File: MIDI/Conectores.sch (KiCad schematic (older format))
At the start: 3 parts, among them J4 CONN_01X06, J5 CONN_01X06

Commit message: Se continuan las correciones correspondientes a la 1ra revisión
> Se realizan los cambios necesarios para la utilización de la biblioteca de huellas autocontenidas.
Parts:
- J4, J5: footprint Pin_Headers:Pin_Header_Straight_1x06_Pitch2.54mm -> MIDI:Pin_Header_Straight_1x06_Pitch2.54mm
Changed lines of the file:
@@
 F 0 "J5" H 6595 2780 50  0000 C CNN
 F 1 "CONN_01X06" V 6695 2430 50  0000 C CNN
-F 2 "Pin_Headers:Pin_Header_Straight_1x06_Pitch2.54mm" H 6595 2430 50  0001 C CNN
+F 2 "MIDI:Pin_Header_Straight_1x06_Pitch2.54mm" H 6595 2430 50  0001 C CNN
 F 3 "http://portal.fciconnect.com/Comergent//fci/drawing/75915.pdf" H 6595 2430 50  0001 C CNN
 F 4 "CONN RCPT 6POS .100\" SGL PCB" H 0   0   60  0001 C CNN "Desc"
@@
 F 0 "J4" H 5045 2780 50  0000 C CNN
 F 1 "CONN_01X06" V 5145 2430 50  0000 C CNN
-F 2 "Pin_Headers:Pin_Header_Straight_1x06_Pitch2.54mm" H 5045 2430 50  0001 C CNN
+F 2 "MIDI:Pin_Header_Straight_1x06_Pitch2.54mm" H 5045 2430 50  0001 C CNN
 F 3 "http://portal.fciconnect.com/Comergent//fci/drawing/75915.pdf" H 5045 2430 50  0001 C CNN
 F 4 "CONN RCPT 6POS .100\" SGL PCB" H 0   0   60  0001 C CNN "Desc"

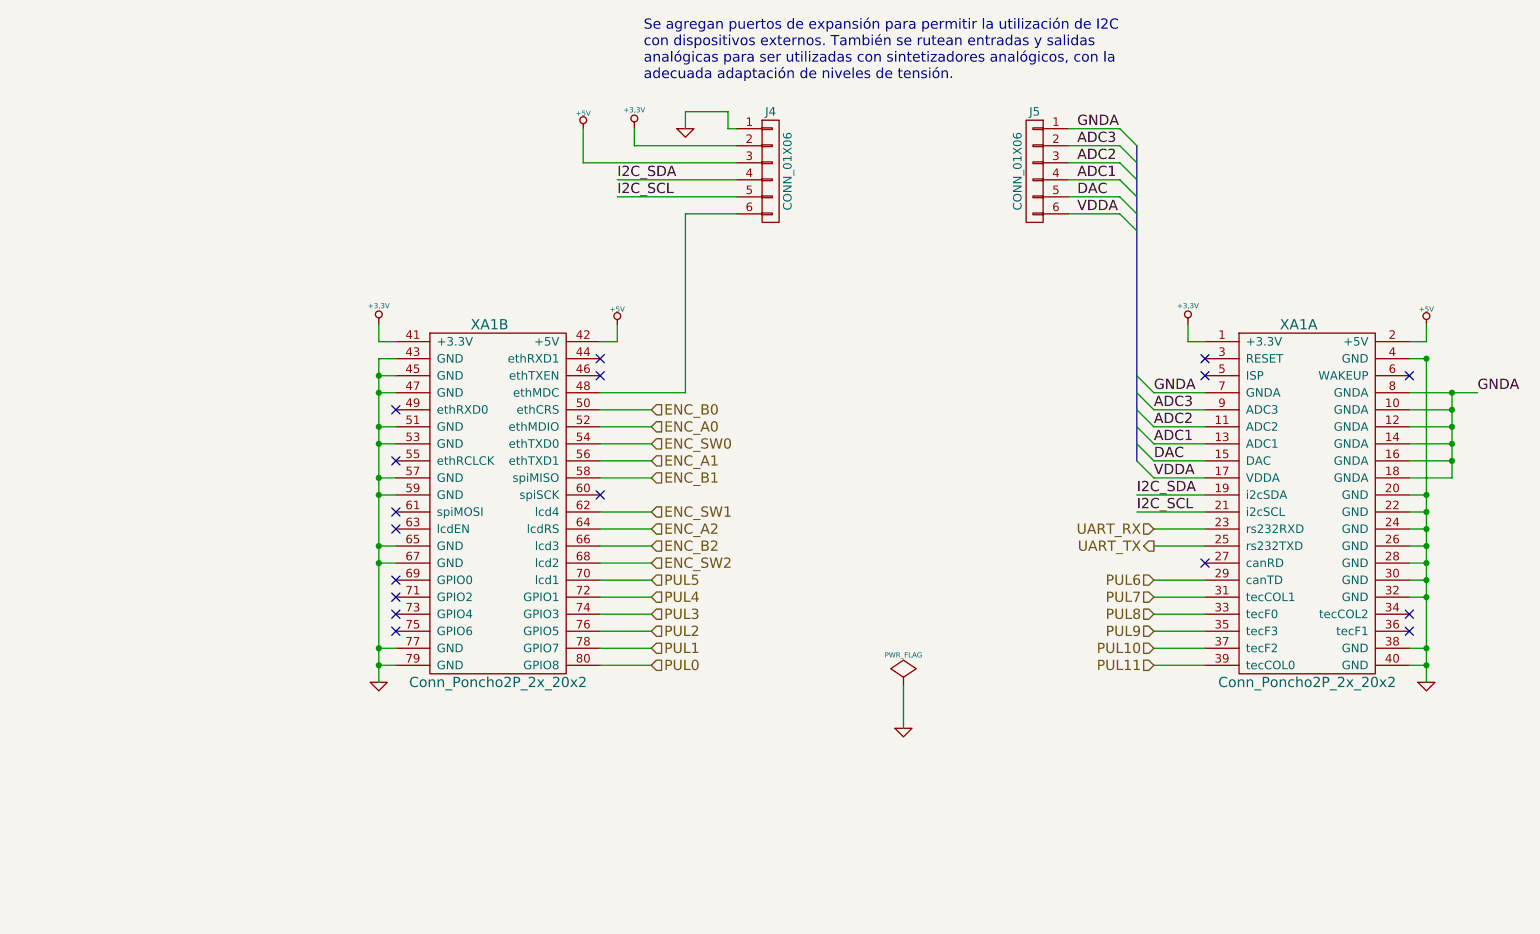
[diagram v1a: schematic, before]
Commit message: Se modifica librería para uncluir tira de pines
> Se reemplaza conector multiparte por elementos individuales para facilitar el cálculo con kiCost.
> Se incluyen modelos 3D para completar la vista 3D.
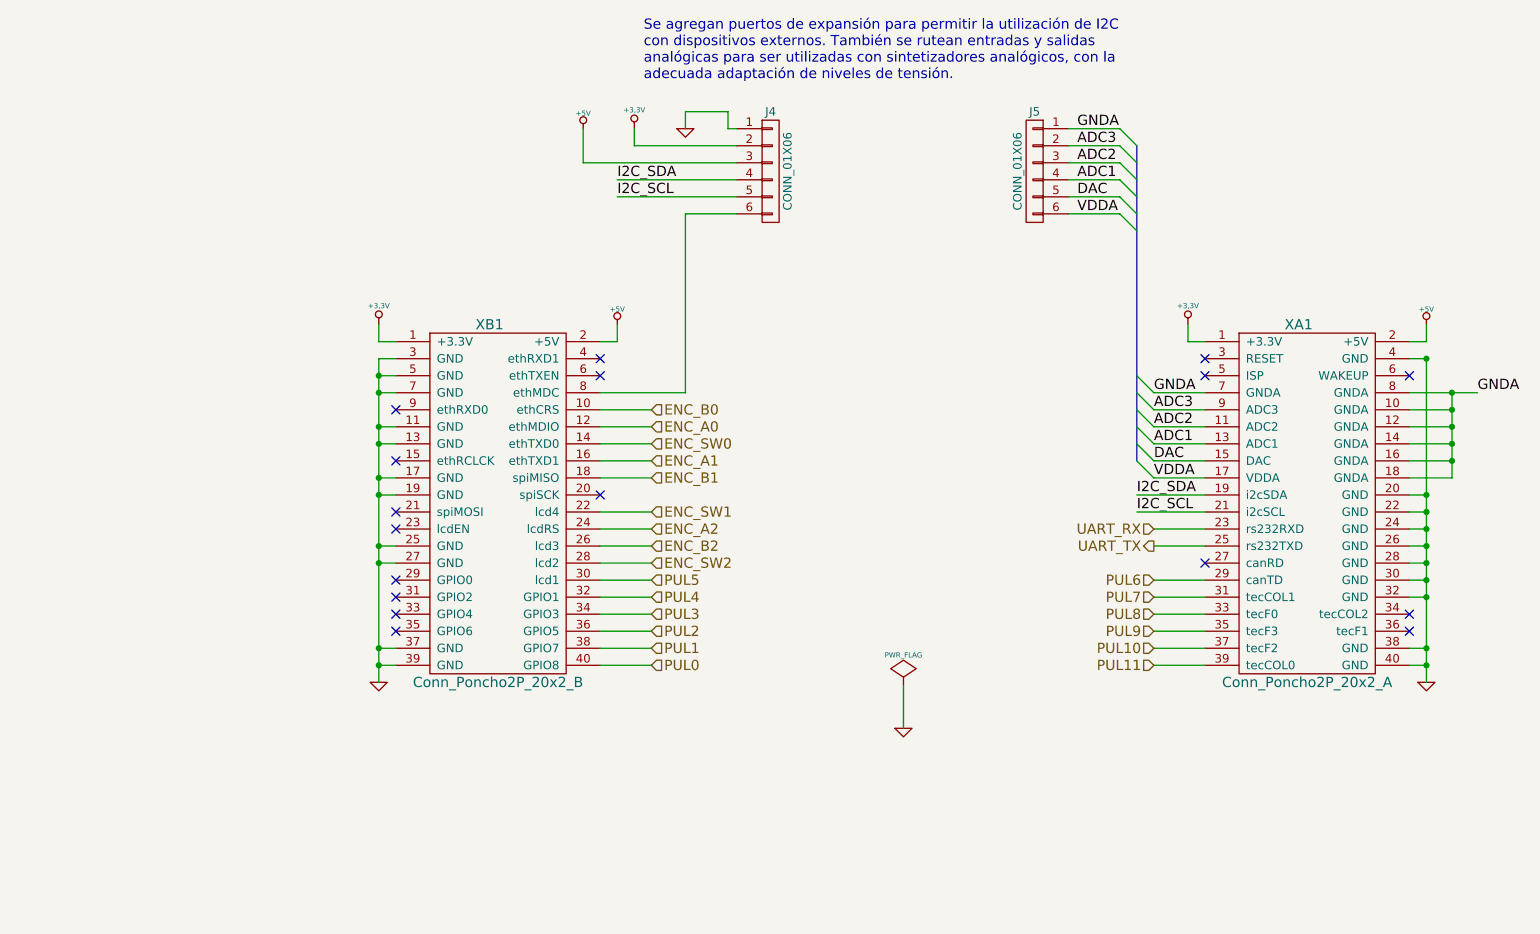
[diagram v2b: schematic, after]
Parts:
- removed XA1: Conn_Poncho2P_2x_20x2, MIDI:Conn_Poncho_Completo, symbol Conn_Poncho2P_2x_20x2
- added XA1: Conn_Poncho2P_20x2_A, MIDI:PIN_ARRAY_20X2, symbol Conn_Poncho2P_20x2_A
- added XB1: Conn_Poncho2P_20x2_B, MIDI:PIN_ARRAY_20X2, symbol Conn_Poncho2P_20x2_B
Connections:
- net +3.3V: now also XA1.1 (+3.3V), XB1.1 (+3.3V)
- net +5V: now also XA1.2 (+5V), XB1.2 (+5V)
- net ADC1: now also XA1.13 (ADC1)
- net ADC2: now also XA1.11 (ADC2)
- net ADC3: now also XA1.9 (ADC3)
- net DAC: now also XA1.15 (DAC)
- net ENC_A0: now also XB1.12 (ethMDIO)
- net ENC_A1: now also XB1.16 (ethTXD1)
- net ENC_A2: now also XB1.24 (lcdRS)
- net ENC_B0: now also XB1.10 (ethCRS)
- net ENC_B1: now also XB1.18 (spiMISO)
- net ENC_B2: now also XB1.26 (lcd3)
- net ENC_SW0: now also XB1.14 (ethTXD0)
- net ENC_SW1: now also XB1.22 (lcd4)
- net ENC_SW2: now also XB1.28 (lcd2)
- net GND: now also XA1.20 (GND), XA1.22 (GND), XA1.24 (GND), XA1.26 (GND), XA1.28 (GND), XA1.30 (GND), XA1.32 (GND), XA1.38 (GND), XA1.4 (GND), XA1.40 (GND), XB1.11 (GND), XB1.13 (GND), XB1.17 (GND), XB1.19 (GND), XB1.25 (GND), XB1.27 (GND), XB1.3 (GND), XB1.37 (GND), XB1.39 (GND), XB1.5 (GND), XB1.7 (GND)
- net GNDA: now also XA1.10 (GNDA), XA1.12 (GNDA), XA1.14 (GNDA), XA1.16 (GNDA), XA1.18 (GNDA), XA1.7 (GNDA), XA1.8 (GNDA)
- net I2C_SCL: now also XA1.21 (i2cSCL)
- net I2C_SDA: now also XA1.19 (i2cSDA)
- net PUL0: now also XB1.40 (GPIO8)
- net PUL1: now also XB1.38 (GPIO7)
- net PUL10: now also XA1.37 (tecF2)
- net PUL11: now also XA1.39 (tecCOL0)
- net PUL2: now also XB1.36 (GPIO5)
- net PUL3: now also XB1.34 (GPIO3)
- net PUL4: now also XB1.32 (GPIO1)
- net PUL5: now also XB1.30 (lcd1)
- net PUL6: now also XA1.29 (canTD)
- net PUL7: now also XA1.31 (tecCOL1)
- net PUL8: now also XA1.33 (tecF0)
- net PUL9: now also XA1.35 (tecF3)
- net UART_RX: now also XA1.23 (rs232RXD)
- net UART_TX: now also XA1.25 (rs232TXD)
- net VDDA: now also XA1.17 (VDDA)
- net at J4.6 (P6): now also XB1.8 (ethMDC)
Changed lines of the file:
@@
 $EndDescr
-$Comp
-L Conn_Poncho2P_2x_20x2 XA1
-U 1 1 592BDB41
-P 7845 3730
-F 0 "XA1" H 8145 4130 60  0000 C CNN
-F 1 "Conn_Poncho2P_2x_20x2" H 8195 2030 60  0000 C CNN
-F 2 "MIDI:Conn_Poncho_Completo" H 7845 3730 60  0001 C CNN
-F 3 "" H 7845 3730 60  0000 C CNN
-	1    7845 3730
-	1    0    0    -1
-$EndComp
-$Comp
-L Conn_Poncho2P_2x_20x2 XA1
-U 2 1 592BDBFC
-P 3095 3730
-F 0 "XA1" H 3395 4130 60  0000 C CNN
-F 1 "Conn_Poncho2P_2x_20x2" H 3445 2030 60  0000 C CNN
-F 2 "MIDI:Conn_Poncho_Completo" H 3095 3730 60  0001 C CNN
-F 3 "" H 3095 3730 60  0000 C CNN
-	2    3095 3730
-	1    0    0    -1
-$EndComp
 $Comp
 L CONN_01X06 J5
@@
 F 3 "" H 2745 5430 60  0000 C CNN
 	1    2745 5430
+	1    0    0    -1
+$EndComp
+$Comp
+L PWR_FLAG #FLG027
+U 1 1 5947169C
+P 5825 5450
+F 0 "#FLG027" H 5825 5545 30  0001 C CNN
+F 1 "PWR_FLAG" H 5825 5630 30  0000 C CNN
+F 2 "" H 5825 5450 60  0000 C CNN
+F 3 "" H 5825 5450 60  0000 C CNN
+	1    5825 5450
+	1    0    0    -1
+$EndComp
+$Comp
+L GND #PWR028
+U 1 1 594716FF
+P 5825 5700
+F 0 "#PWR028" H 5825 5700 30  0001 C CNN
+F 1 "GND" H 5825 5630 30  0001 C CNN
+F 2 "" H 5825 5700 60  0000 C CNN
+F 3 "" H 5825 5700 60  0000 C CNN
+	1    5825 5700
+	1    0    0    -1
+$EndComp
+$Comp
+L Conn_Poncho2P_20x2_B XB1
+U 1 1 5966AC2D
+P 3095 3730
+F 0 "XB1" H 3395 4130 60  0000 C CNN
+F 1 "Conn_Poncho2P_20x2_B" H 3445 2030 60  0000 C CNN
+F 2 "MIDI:PIN_ARRAY_20X2" H 3095 3730 60  0001 C CNN
+F 3 "http://portal.fciconnect.com/Comergent//fci/drawing/67996.pdf" H 3095 3730 60  0001 C CNN
+F 4 "BERGSTIK II 0.100\" DUAL ST" H 0   0   60  0001 C CNN "Desc"
+F 5 "609-4724-ND" H 0   0   50  0001 C CNN "Digikey#"
+F 6 "Amphenol FCI" H 0   0   50  0001 C CNN "Manf"
+F 7 "68602-140HLF" H 0   0   50  0001 C CNN "Manf#"
+F 8 "649-68602-140HLF" H 0   0   50  0001 C CNN "Mouser#"
+	1    3095 3730
+	1    0    0    -1
+$EndComp
+$Comp
+L Conn_Poncho2P_20x2_A XA1
+U 1 1 5966ACA6
+P 7845 3730
+F 0 "XA1" H 8145 4130 60  0000 C CNN
+F 1 "Conn_Poncho2P_20x2_A" H 8195 2030 60  0000 C CNN
+F 2 "MIDI:PIN_ARRAY_20X2" H 7845 3730 60  0001 C CNN
+F 3 "http://portal.fciconnect.com/Comergent//fci/drawing/67996.pdf" H 7845 3730 60  0001 C CNN
+F 4 "BERGSTIK II 0.100\" DUAL ST" H 0   0   60  0001 C CNN "Desc"
+F 5 "609-4724-ND" H 0   0   50  0001 C CNN "Digikey#"
+F 6 "Amphenol FCI" H 0   0   50  0001 C CNN "Manf"
+F 7 "68602-140HLF" H 0   0   50  0001 C CNN "Manf#"
+F 8 "649-68602-140HLF" H 0   0   50  0001 C CNN "Mouser#"
+	1    7845 3730
 	1    0    0    -1
 $EndComp
@@
 Wire Wire Line
 	2845 3630 2745 3630
+Wire Wire Line
+	8895 3530 8895 5430
+Wire Wire Line
+	8895 3430 8895 3330
+Wire Wire Line
+	5825 5450 5825 5700
 Entry Wire Line
 	7195 3630 7295 3730
@@
 NoConn ~ 4045 3530
 NoConn ~ 4045 3630
-Wire Wire Line
-	8895 3530 8895 5430
-Wire Wire Line
-	8895 3430 8895 3330
-$Comp
-L PWR_FLAG #FLG027
-U 1 1 5947169C
-P 5825 5450
-F 0 "#FLG027" H 5825 5545 30  0001 C CNN
-F 1 "PWR_FLAG" H 5825 5630 30  0000 C CNN
-F 2 "" H 5825 5450 60  0000 C CNN
-F 3 "" H 5825 5450 60  0000 C CNN
-	1    5825 5450
-	1    0    0    -1
-$EndComp
-$Comp
-L GND #PWR028
-U 1 1 594716FF
-P 5825 5700
-F 0 "#PWR028" H 5825 5700 30  0001 C CNN
-F 1 "GND" H 5825 5630 30  0001 C CNN
-F 2 "" H 5825 5700 60  0000 C CNN
-F 3 "" H 5825 5700 60  0000 C CNN
-	1    5825 5700
-	1    0    0    -1
-$EndComp
-Wire Wire Line
-	5825 5450 5825 5700
 $EndSCHEMATC

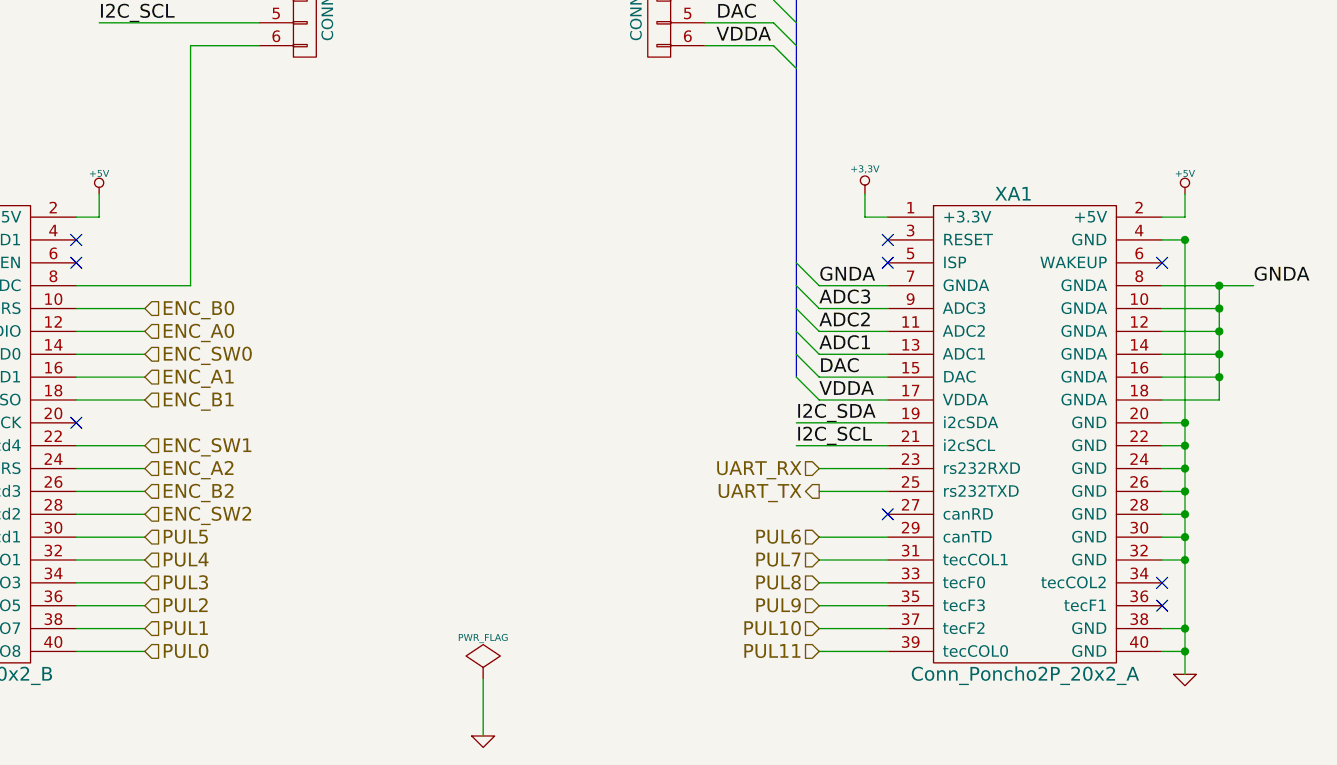
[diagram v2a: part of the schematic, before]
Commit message: Se avanza con primera iteración de ruteo
> Se terminan de rutear conexiones para estudiar factibilidad de placement.
> Para facilitar el ruteo se realizan los siguientes cambios:
  > Se desconecta pin redundante de tact-switch's para permitir la conexión entre planos de masa.
  > Se desconectan pines del conector derecho de forma que no requieran ser ruteados a los homologos del conector izquierdo.
  > Se intercambian unidades F y D del componente 40106.
  > Se agrupan señales de los interruptores de los encoders en vez de intercalarlos con las señales de encoder, propiamente dicho, de cada uno. Se rutean a pines superiores en el conector izquierdo, mientras se desplazan las restantes señales hacia abajo.

> Se aguarda comentarios de los revisores para emprolijar, embellecer y mejorar el ruteo.
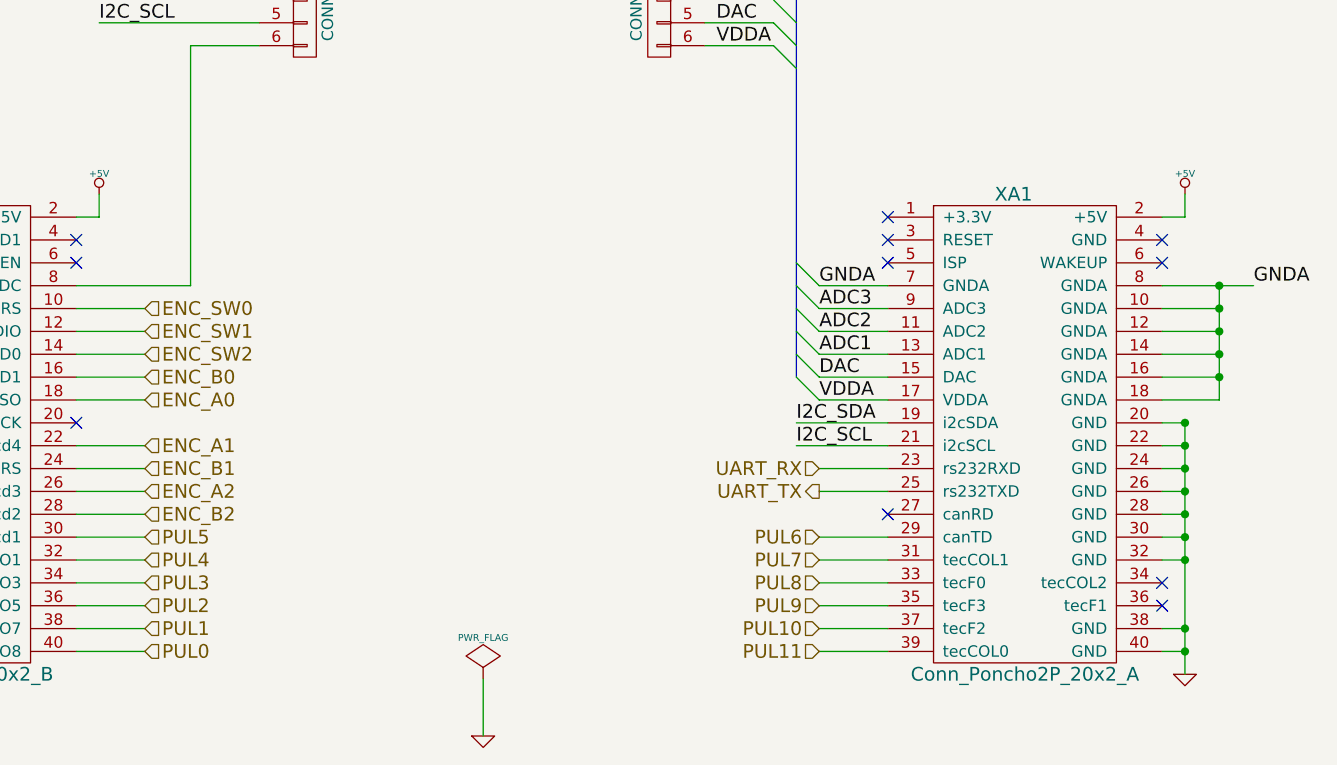
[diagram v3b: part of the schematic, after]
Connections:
- net +3.3V: no longer XA1.1 (+3.3V)
- net ENC_A0: now also XB1.18 (spiMISO); no longer XB1.12 (ethMDIO)
- net ENC_A1: now also XB1.22 (lcd4); no longer XB1.16 (ethTXD1)
- net ENC_A2: now also XB1.26 (lcd3); no longer XB1.24 (lcdRS)
- net ENC_B0: now also XB1.16 (ethTXD1); no longer XB1.10 (ethCRS)
- net ENC_B1: now also XB1.24 (lcdRS); no longer XB1.18 (spiMISO)
- net ENC_B2: now also XB1.28 (lcd2); no longer XB1.26 (lcd3)
- net ENC_SW0: now also XB1.10 (ethCRS); no longer XB1.14 (ethTXD0)
- net ENC_SW1: now also XB1.12 (ethMDIO); no longer XB1.22 (lcd4)
- net ENC_SW2: now also XB1.14 (ethTXD0); no longer XB1.28 (lcd2)
- net GND: no longer XA1.4 (GND)
- no-connect marks 17 -> 19
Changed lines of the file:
@@
 $EndComp
 $Comp
-L +3,3V #PWR024
-U 1 1 592C8049
-P 7495 3330
-F 0 "#PWR024" H 7495 3290 30  0001 C CNN
-F 1 "+3,3V" H 7495 3440 30  0000 C CNN
-F 2 "" H 7495 3330 60  0000 C CNN
-F 3 "" H 7495 3330 60  0000 C CNN
-	1    7495 3330
-	1    0    0    -1
-$EndComp
-$Comp
-L GND #PWR025
+L GND #PWR024
 U 1 1 592C811E
 P 8895 5430
-F 0 "#PWR025" H 8895 5430 30  0001 C CNN
+F 0 "#PWR024" H 8895 5430 30  0001 C CNN
 F 1 "GND" H 8895 5360 30  0001 C CNN
 F 2 "" H 8895 5430 60  0000 C CNN
@@
 $EndComp
 $Comp
-L GND #PWR026
+L GND #PWR025
 U 1 1 592C87A2
 P 2745 5430
-F 0 "#PWR026" H 2745 5430 30  0001 C CNN
+F 0 "#PWR025" H 2745 5430 30  0001 C CNN
 F 1 "GND" H 2745 5360 30  0001 C CNN
 F 2 "" H 2745 5430 60  0000 C CNN
@@
 $EndComp
 $Comp
-L PWR_FLAG #FLG027
+L PWR_FLAG #FLG026
 U 1 1 5947169C
 P 5825 5450
-F 0 "#FLG027" H 5825 5545 30  0001 C CNN
+F 0 "#FLG026" H 5825 5545 30  0001 C CNN
 F 1 "PWR_FLAG" H 5825 5630 30  0000 C CNN
 F 2 "" H 5825 5450 60  0000 C CNN
@@
 $EndComp
 $Comp
-L GND #PWR028
+L GND #PWR027
 U 1 1 594716FF
 P 5825 5700
-F 0 "#PWR028" H 5825 5700 30  0001 C CNN
+F 0 "#PWR027" H 5825 5700 30  0001 C CNN
 F 1 "GND" H 5825 5630 30  0001 C CNN
 F 2 "" H 5825 5700 60  0000 C CNN
@@
 Text Label 7195 4430 0    60   ~ 0
 I2C_SCL
+Text HLabel 4345 4030 2    60   Input ~ 0
+ENC_SW2
+Text HLabel 4345 3930 2    60   Input ~ 0
+ENC_SW1
+Text HLabel 4345 3830 2    60   Input ~ 0
+ENC_SW0
+Text HLabel 4345 4630 2    60   Input ~ 0
+ENC_A2
 Text HLabel 4345 4730 2    60   Input ~ 0
-ENC_SW2
+ENC_B2
 Text HLabel 4345 4430 2    60   Input ~ 0
-ENC_SW1
-Text HLabel 4345 4030 2    60   Input ~ 0
-ENC_SW0
+ENC_A1
 Text HLabel 4345 4530 2    60   Input ~ 0
-ENC_A2
-Text HLabel 4345 4630 2    60   Input ~ 0
-ENC_B2
+ENC_B1
+Text HLabel 4345 4230 2    60   Input ~ 0
+ENC_A0
 Text HLabel 4345 4130 2    60   Input ~ 0
-ENC_A1
-Text HLabel 4345 4230 2    60   Input ~ 0
-ENC_B1
-Text HLabel 4345 3930 2    60   Input ~ 0
-ENC_A0
-Text HLabel 4345 3830 2    60   Input ~ 0
 ENC_B0
 Text Label 4145 2480 0    60   ~ 0
@@
 	4145 3430 4145 3330
 Wire Wire Line
-	7495 3330 7495 3430
-Wire Wire Line
-	7495 3430 7595 3430
-Wire Wire Line
 	8795 3430 8895 3430
 Wire Wire Line
-	8795 3530 8895 3530
-Wire Wire Line
 	8795 5330 8895 5330
 Wire Wire Line
@@
 	2845 3630 2745 3630
 Wire Wire Line
-	8895 3530 8895 5430
-Wire Wire Line
 	8895 3430 8895 3330
 Wire Wire Line
@@
 Entry Wire Line
 	7095 2680 7195 2780
-Connection ~ 8895 3530
 Connection ~ 8895 5330
 Connection ~ 8895 5230
@@
 NoConn ~ 4045 3530
 NoConn ~ 4045 3630
+NoConn ~ 7595 3430
+NoConn ~ 8795 3530
+Wire Wire Line
+	8895 4330 8895 5430
 $EndSCHEMATC
